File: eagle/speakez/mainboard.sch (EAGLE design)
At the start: 42 parts, among them U1 +12v

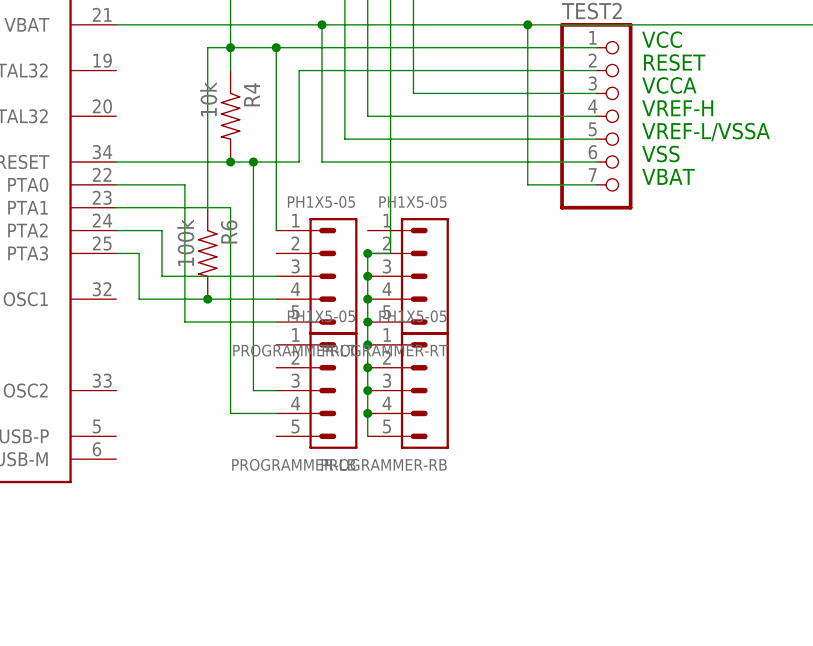
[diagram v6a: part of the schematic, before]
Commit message: 0.05" header to 0.1" header
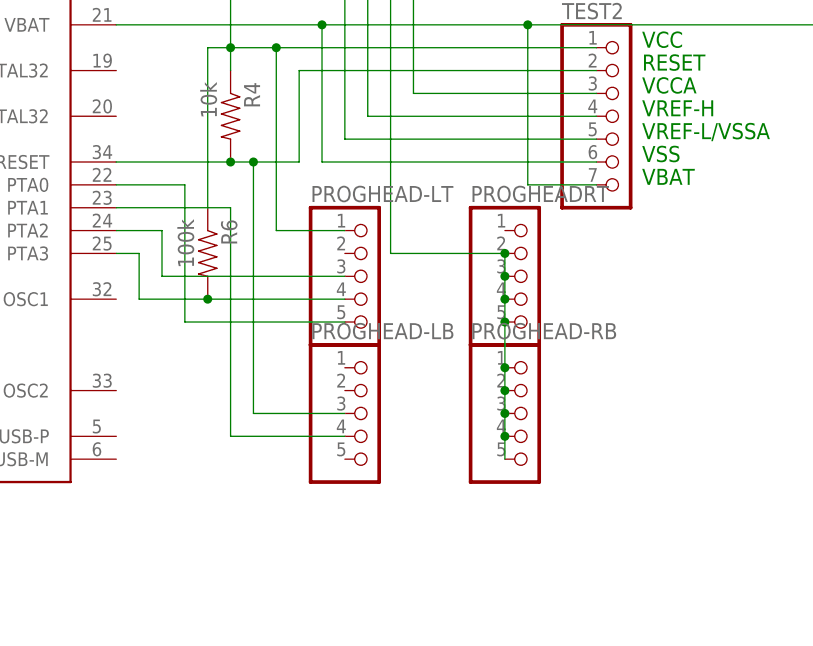
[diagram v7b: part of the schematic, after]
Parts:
- removed PROGRAMMER-LB, PROGRAMMER-LT, PROGRAMMER-RB, PROGRAMMER-RT: PH1X5-05, pel_hdr:PH1X5-05
- added PROGHEAD-LB, PROGHEAD-LT, PROGHEAD-RB, PROGHEADRT: (no value), pinhead:PINHD-1X5
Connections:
- net GND: now also PROGHEAD-RB.1, PROGHEAD-RB.2, PROGHEAD-RB.3, PROGHEAD-RB.4, PROGHEAD-RB.5, PROGHEADRT.2, PROGHEADRT.3, PROGHEADRT.4, PROGHEADRT.5; no longer PROGRAMMER-RB.1, PROGRAMMER-RB.2, PROGRAMMER-RB.3, PROGRAMMER-RB.4, PROGRAMMER-RB.5, PROGRAMMER-RT.2, PROGRAMMER-RT.3, PROGRAMMER-RT.4, PROGRAMMER-RT.5
- net N$14: now also PROGHEAD-LT.5; no longer PROGRAMMER-LT.5
- net N$20: now also PROGHEAD-LB.3; no longer PROGRAMMER-LB.3
- net N$21: now also PROGHEAD-LB.4; no longer PROGRAMMER-LB.4
- net N$23: now also PROGHEAD-LT.3; no longer PROGRAMMER-LT.3
- net N$24: now also PROGHEAD-LT.4; no longer PROGRAMMER-LT.4
- net N$3: now also PROGHEAD-LT.1; no longer PROGRAMMER-LT.1
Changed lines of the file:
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@@
 <part name="SUPPLY3" library="supply2" deviceset="GND" device=""/>
 <part name="R4" library="SparkFun-Passives" deviceset="RESISTOR" device="0805-RES" value="10k"/>
-<part name="PROGRAMMER-LT" library="pel_hdr" deviceset="PH1X5" device="-05"/>
 <part name="SERIAL" library="pinhead" deviceset="PINHD-1X4" device=""/>
 <part name="R5" library="SparkFun-Passives" deviceset="RESISTOR" device="0805-RES" value="50k"/>
@@
 <part name="SUPPLY5" library="supply2" deviceset="GND" device=""/>
 <part name="TEST2" library="pinhead" deviceset="PINHD-1X7" device=""/>
-<part name="PROGRAMMER-LB" library="pel_hdr" deviceset="PH1X5" device="-05"/>
-<part name="PROGRAMMER-RT" library="pel_hdr" deviceset="PH1X5" device="-05"/>
-<part name="PROGRAMMER-RB" library="pel_hdr" deviceset="PH1X5" device="-05"/>
 <part name="R6" library="SparkFun-Passives" deviceset="RESISTOR" device="0805-RES" value="100k"/>
 <part name="C10" library="SparkFun-Capacitors" deviceset="CAP" device="0805" value="0.1uF"/>
@@
 <part name="BK2125HM601-T1" library="SparkFun-Passives" deviceset="INDUCTOR" device="0805"/>
 <part name="SUPPLY9" library="supply2" deviceset="GND" device=""/>
+<part name="PROGHEADRT" library="pinhead" deviceset="PINHD-1X5" device=""/>
+<part name="PROGHEAD-RB" library="pinhead" deviceset="PINHD-1X5" device=""/>
+<part name="PROGHEAD-LT" library="pinhead" deviceset="PINHD-1X5" device=""/>
+<part name="PROGHEAD-LB" library="pinhead" deviceset="PINHD-1X5" device=""/>
 </parts>
 <sheets>
@@
 <instance part="SUPPLY3" gate="GND" x="99.06" y="5.08"/>
 <instance part="R4" gate="G$1" x="187.96" y="5.08" rot="R270"/>
-<instance part="PROGRAMMER-LT" gate="G$1" x="200.66" y="-7.62" rot="R180"/>
 <instance part="SERIAL" gate="A" x="96.52" y="-7.62" rot="R180"/>
 <instance part="R5" gate="G$1" x="106.68" y="-38.1" rot="R90"/>
@@
 <instance part="SUPPLY5" gate="GND" x="106.68" y="-48.26"/>
 <instance part="TEST2" gate="A" x="231.14" y="5.08"/>
-<instance part="PROGRAMMER-LB" gate="G$1" x="200.66" y="-20.32" rot="R180"/>
-<instance part="PROGRAMMER-RT" gate="G$1" x="210.82" y="-7.62" rot="R180"/>
-<instance part="PROGRAMMER-RB" gate="G$1" x="210.82" y="-20.32" rot="R180"/>
 <instance part="R6" gate="G$1" x="185.42" y="-10.16" rot="R270"/>
 <instance part="C10" gate="G$1" x="193.04" y="58.42"/>
@@
 <instance part="BK2125HM601-T1" gate="G$1" x="243.84" y="27.94" rot="R90"/>
 <instance part="SUPPLY9" gate="GND" x="251.46" y="25.4"/>
+<instance part="PROGHEADRT" gate="A" x="220.98" y="-12.7"/>
+<instance part="PROGHEAD-RB" gate="A" x="220.98" y="-27.94"/>
+<instance part="PROGHEAD-LT" gate="A" x="203.2" y="-12.7"/>
+<instance part="PROGHEAD-LB" gate="A" x="203.2" y="-27.94"/>
 </instances>
 <busses>
@@
 <pinref part="C12" gate="G$1" pin="2"/>
 <wire x1="210.82" y1="55.88" x2="223.52" y2="55.88" width="0.1524" layer="91"/>
-<pinref part="PROGRAMMER-RT" gate="G$1" pin="2"/>
-<pinref part="PROGRAMMER-RT" gate="G$1" pin="3"/>
-<wire x1="203.2" y1="-10.16" x2="203.2" y2="-12.7" width="0.1524" layer="91"/>
-<pinref part="PROGRAMMER-RT" gate="G$1" pin="4"/>
-<wire x1="203.2" y1="-15.24" x2="203.2" y2="-12.7" width="0.1524" layer="91"/>
-<junction x="203.2" y="-12.7"/>
-<pinref part="PROGRAMMER-RT" gate="G$1" pin="5"/>
-<wire x1="203.2" y1="-15.24" x2="203.2" y2="-17.78" width="0.1524" layer="91"/>
-<junction x="203.2" y="-15.24"/>
-<pinref part="PROGRAMMER-RB" gate="G$1" pin="1"/>
-<wire x1="203.2" y1="-17.78" x2="203.2" y2="-20.32" width="0.1524" layer="91"/>
-<junction x="203.2" y="-17.78"/>
-<pinref part="PROGRAMMER-RB" gate="G$1" pin="2"/>
-<wire x1="203.2" y1="-20.32" x2="203.2" y2="-22.86" width="0.1524" layer="91"/>
-<junction x="203.2" y="-20.32"/>
-<pinref part="PROGRAMMER-RB" gate="G$1" pin="3"/>
-<wire x1="203.2" y1="-22.86" x2="203.2" y2="-25.4" width="0.1524" layer="91"/>
-<junction x="203.2" y="-22.86"/>
-<pinref part="PROGRAMMER-RB" gate="G$1" pin="4"/>
-<wire x1="203.2" y1="-25.4" x2="203.2" y2="-27.94" width="0.1524" layer="91"/>
-<junction x="203.2" y="-25.4"/>
-<pinref part="PROGRAMMER-RB" gate="G$1" pin="5"/>
-<wire x1="203.2" y1="-27.94" x2="203.2" y2="-30.48" width="0.1524" layer="91"/>
-<junction x="203.2" y="-27.94"/>
 <pinref part="BATTERY" gate="G$1" pin="2"/>
 <wire x1="129.54" y1="109.22" x2="129.54" y2="106.68" width="0.1524" layer="91"/>
@@
 <pinref part="SERIAL" gate="A" pin="4"/>
 <wire x1="109.22" y1="-5.08" x2="99.06" y2="-5.08" width="0.1524" layer="91"/>
-<wire x1="203.2" y1="-10.16" x2="205.74" y2="-10.16" width="0.1524" layer="91"/>
 <wire x1="205.74" y1="-10.16" x2="205.74" y2="20.32" width="0.1524" layer="91"/>
-<junction x="203.2" y="-10.16"/>
 <junction x="205.74" y="20.32"/>
 <wire x1="210.82" y1="55.88" x2="205.74" y2="55.88" width="0.1524" layer="91"/>
@@
 <pinref part="SUPPLY7" gate="GND" pin="GND"/>
 <junction x="134.62" y="83.82"/>
+<pinref part="PROGHEADRT" gate="A" pin="2"/>
+<pinref part="PROGHEADRT" gate="A" pin="3"/>
+<wire x1="218.44" y1="-10.16" x2="218.44" y2="-12.7" width="0.1524" layer="91"/>
+<pinref part="PROGHEADRT" gate="A" pin="4"/>
+<wire x1="218.44" y1="-15.24" x2="218.44" y2="-12.7" width="0.1524" layer="91"/>
+<junction x="218.44" y="-12.7"/>
+<pinref part="PROGHEADRT" gate="A" pin="5"/>
+<wire x1="218.44" y1="-17.78" x2="218.44" y2="-15.24" width="0.1524" layer="91"/>
+<junction x="218.44" y="-15.24"/>
+<pinref part="PROGHEAD-RB" gate="A" pin="1"/>
+<wire x1="218.44" y1="-17.78" x2="218.44" y2="-22.86" width="0.1524" layer="91"/>
+<junction x="218.44" y="-17.78"/>
+<pinref part="PROGHEAD-RB" gate="A" pin="2"/>
+<wire x1="218.44" y1="-22.86" x2="218.44" y2="-25.4" width="0.1524" layer="91"/>
+<junction x="218.44" y="-22.86"/>
+<pinref part="PROGHEAD-RB" gate="A" pin="3"/>
+<wire x1="218.44" y1="-25.4" x2="218.44" y2="-27.94" width="0.1524" layer="91"/>
+<junction x="218.44" y="-25.4"/>
+<pinref part="PROGHEAD-RB" gate="A" pin="4"/>
+<wire x1="218.44" y1="-27.94" x2="218.44" y2="-30.48" width="0.1524" layer="91"/>
+<junction x="218.44" y="-27.94"/>
+<pinref part="PROGHEAD-RB" gate="A" pin="5"/>
+<wire x1="218.44" y1="-30.48" x2="218.44" y2="-33.02" width="0.1524" layer="91"/>
+<junction x="218.44" y="-30.48"/>
+<wire x1="205.74" y1="-10.16" x2="218.44" y2="-10.16" width="0.1524" layer="91"/>
+<junction x="218.44" y="-10.16"/>
 </segment>
 <segment>
@@
 <wire x1="228.6" y1="12.7" x2="193.04" y2="12.7" width="0.1524" layer="91"/>
 <junction x="187.96" y="12.7"/>
-<pinref part="PROGRAMMER-LT" gate="G$1" pin="1"/>
 <wire x1="193.04" y1="12.7" x2="187.96" y2="12.7" width="0.1524" layer="91"/>
 <wire x1="193.04" y1="-7.62" x2="193.04" y2="12.7" width="0.1524" layer="91"/>
@@
 <pinref part="TEST2" gate="A" pin="7"/>
 <wire x1="220.98" y1="-2.54" x2="228.6" y2="-2.54" width="0.1524" layer="91"/>
+<pinref part="PROGHEAD-LT" gate="A" pin="1"/>
+<wire x1="193.04" y1="-7.62" x2="200.66" y2="-7.62" width="0.1524" layer="91"/>
 </segment>
 </net>
@@
 <wire x1="195.58" y1="10.16" x2="195.58" y2="0" width="0.1524" layer="91"/>
 <wire x1="228.6" y1="10.16" x2="195.58" y2="10.16" width="0.1524" layer="91"/>
-<wire x1="190.5" y1="0" x2="190.5" y2="-25.4" width="0.1524" layer="91"/>
+<wire x1="190.5" y1="0" x2="190.5" y2="-27.94" width="0.1524" layer="91"/>
 <junction x="190.5" y="0"/>
-<pinref part="PROGRAMMER-LB" gate="G$1" pin="3"/>
-<wire x1="190.5" y1="-25.4" x2="193.04" y2="-25.4" width="0.1524" layer="91"/>
+<pinref part="PROGHEAD-LB" gate="A" pin="3"/>
+<wire x1="190.5" y1="-27.94" x2="200.66" y2="-27.94" width="0.1524" layer="91"/>
 </segment>
 </net>
@@
 <wire x1="175.26" y1="-7.62" x2="180.34" y2="-7.62" width="0.1524" layer="91"/>
 <wire x1="180.34" y1="-7.62" x2="180.34" y2="-12.7" width="0.1524" layer="91"/>
-<pinref part="PROGRAMMER-LT" gate="G$1" pin="3"/>
-<wire x1="193.04" y1="-12.7" x2="180.34" y2="-12.7" width="0.1524" layer="91"/>
+<wire x1="200.66" y1="-12.7" x2="180.34" y2="-12.7" width="0.1524" layer="91"/>
+<pinref part="PROGHEAD-LT" gate="A" pin="3"/>
 </segment>
 </net>
@@
 <wire x1="175.26" y1="-10.16" x2="177.8" y2="-10.16" width="0.1524" layer="91"/>
 <wire x1="177.8" y1="-10.16" x2="177.8" y2="-15.24" width="0.1524" layer="91"/>
-<pinref part="PROGRAMMER-LT" gate="G$1" pin="4"/>
-<wire x1="193.04" y1="-15.24" x2="185.42" y2="-15.24" width="0.1524" layer="91"/>
 <pinref part="R6" gate="G$1" pin="2"/>
 <wire x1="185.42" y1="-15.24" x2="177.8" y2="-15.24" width="0.1524" layer="91"/>
 <junction x="185.42" y="-15.24"/>
+<pinref part="PROGHEAD-LT" gate="A" pin="4"/>
+<wire x1="185.42" y1="-15.24" x2="200.66" y2="-15.24" width="0.1524" layer="91"/>
 </segment>
 </net>
@@
 <wire x1="175.26" y1="-2.54" x2="182.88" y2="-2.54" width="0.1524" layer="91"/>
 <wire x1="182.88" y1="-2.54" x2="182.88" y2="-17.78" width="0.1524" layer="91"/>
-<pinref part="PROGRAMMER-LT" gate="G$1" pin="5"/>
-<wire x1="182.88" y1="-17.78" x2="193.04" y2="-17.78" width="0.1524" layer="91"/>
+<wire x1="182.88" y1="-17.78" x2="200.66" y2="-17.78" width="0.1524" layer="91"/>
+<pinref part="PROGHEAD-LT" gate="A" pin="5"/>
 </segment>
 </net>
@@
 <pinref part="U$1" gate="G$1" pin="PTA1"/>
 <wire x1="175.26" y1="-5.08" x2="187.96" y2="-5.08" width="0.1524" layer="91"/>
-<wire x1="187.96" y1="-5.08" x2="187.96" y2="-27.94" width="0.1524" layer="91"/>
-<pinref part="PROGRAMMER-LB" gate="G$1" pin="4"/>
-<wire x1="187.96" y1="-27.94" x2="193.04" y2="-27.94" width="0.1524" layer="91"/>
-</segment>
-</net>
+<wire x1="187.96" y1="-5.08" x2="187.96" y2="-30.48" width="0.1524" layer="91"/>
+<pinref part="PROGHEAD-LB" gate="A" pin="4"/>
+<wire x1="187.96" y1="-30.48" x2="200.66" y2="-30.48" width="0.1524" layer="91"/>
+</segment>
+</net>

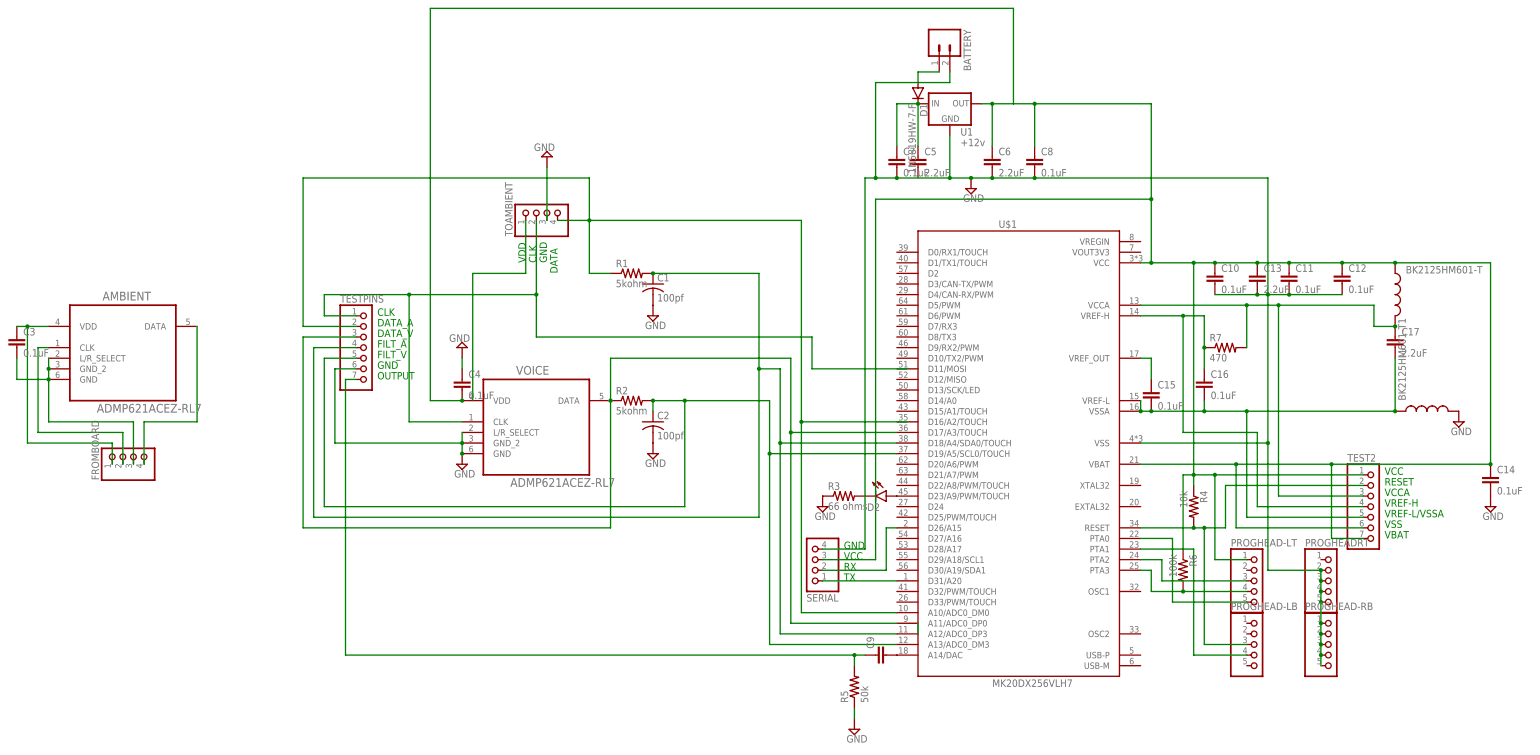
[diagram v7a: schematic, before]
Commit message: update jlink connector
also add jtag support
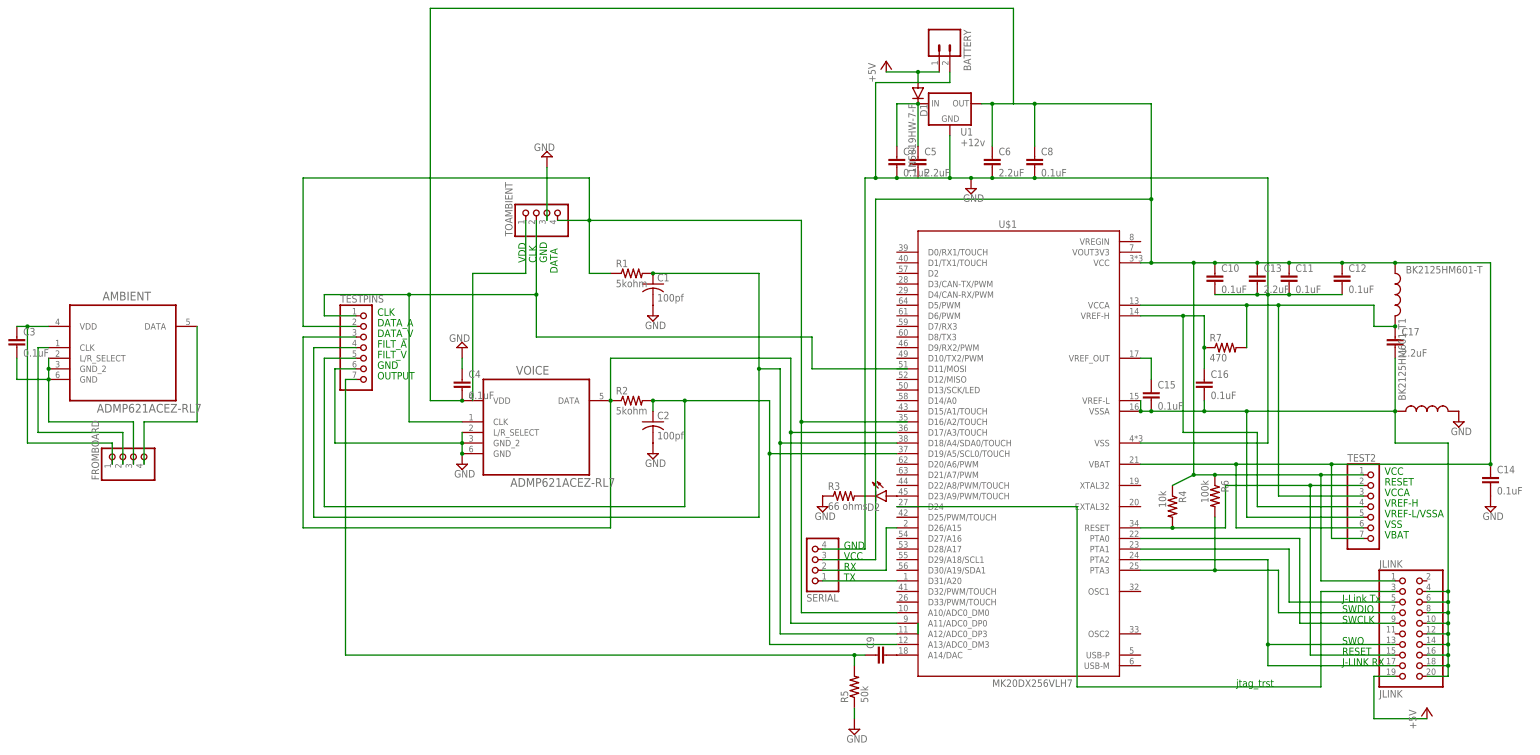
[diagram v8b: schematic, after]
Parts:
- removed PROGHEAD-LB, PROGHEAD-LT, PROGHEAD-RB, PROGHEADRT: (no value), pinhead:PINHD-1X5
- added JLINK: JLINK, pinhead:PINHD-2X10
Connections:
- removed net N$20: PROGHEAD-LB.3, R4.2, TEST2.2, U$1.RESET
- removed net N$21: PROGHEAD-LB.4, U$1.PTA1
- new net +5V: BATTERY.1, D1.A, JLINK.19
- new net N$16: JLINK.3, U$1.D24
- new net RESET: JLINK.15, R4.2, TEST2.2, U$1.RESET
- net GND: no longer PROGHEAD-RB.1, PROGHEAD-RB.2, PROGHEAD-RB.3, PROGHEAD-RB.4, PROGHEAD-RB.5, PROGHEADRT.2, PROGHEADRT.3, PROGHEADRT.4, PROGHEADRT.5
- net N$13: now also JLINK.5, U$1.PTA1; no longer BATTERY.1, D1.A
- net N$14: now also JLINK.9; no longer PROGHEAD-LT.5
- net N$23: now also JLINK.13, JLINK.17; no longer PROGHEAD-LT.3
- net N$24: now also JLINK.7; no longer PROGHEAD-LT.4
- net N$29: now also JLINK.10, JLINK.12, JLINK.14, JLINK.16, JLINK.18, JLINK.20, JLINK.4, JLINK.6, JLINK.8
- net N$3: now also JLINK.1; no longer PROGHEAD-LT.1
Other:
- note added: "J-LINK RX"
- note added: "J-Link Tx"
- note added: "SWCLK"
- note added: "SWDIO"
- note added: "SWO"
- note added: "jtag_trst"
- moved on the sheet: R4, R6
